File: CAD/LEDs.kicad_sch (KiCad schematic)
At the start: 12 parts

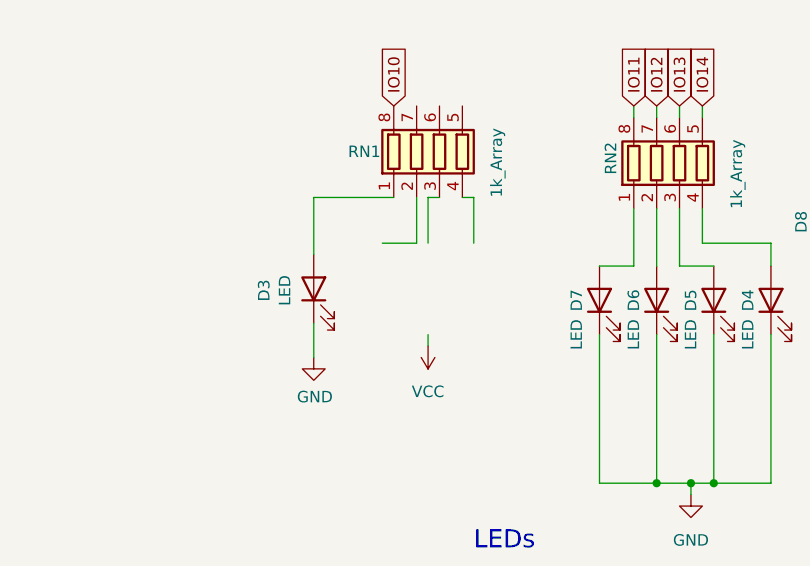
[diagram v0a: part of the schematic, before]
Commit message: Removed RN1
Removed RN1 since only one value was used. Changed to single 1k resistor
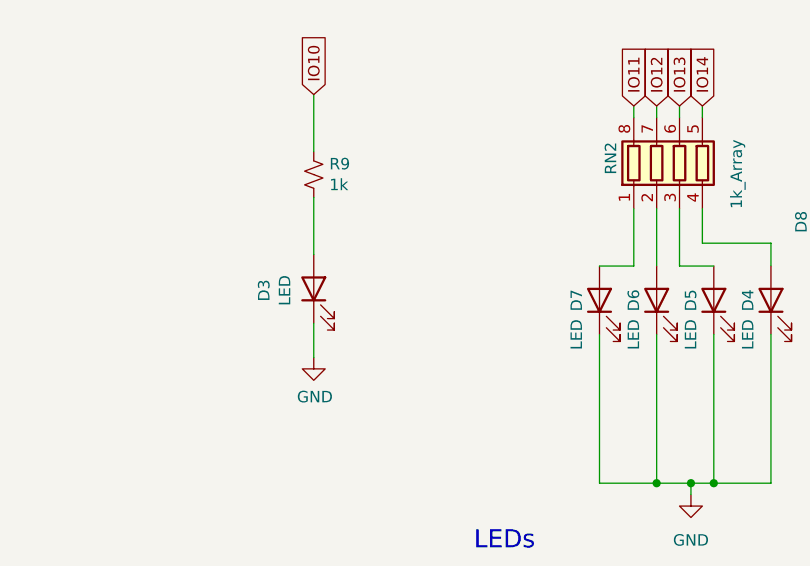
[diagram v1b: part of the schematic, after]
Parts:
- removed RN1: 1k_Array, BadgePirates:R_Array_Convex_4x0603, symbol Device:R_Pack04
- added R9: 1k, BadgePirates:R_1206_3216Metric, symbol Device:R_Small_US
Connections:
- net IO10: now also R9.1
- net at D3.2 (A): now also R9.2
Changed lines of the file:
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@@
-    (stroke (width 0) (type default))
-  )
-  (wire (pts (xy 132.08 86.36) (xy 135.89 86.36))
     (stroke (width 0) (type default))
   )
@@
     (stroke (width 0) (type default))
   )
-  (wire (pts (xy 142.24 81.28) (xy 140.97 81.28))
-    (stroke (width 0) (type default))
-  )
   (wire (pts (xy 165.1 71.12) (xy 165.1 72.39))
     (stroke (width 0) (type default))
@@
     (stroke (width 0) (type default))
   )
-  (wire (pts (xy 137.16 81.28) (xy 138.43 81.28))
-    (stroke (width 0) (type default))
-  )
   (wire (pts (xy 55.88 116.84) (xy 55.88 121.92))
     (stroke (width 0) (type default))
@@
     (stroke (width 0) (type default))
   )
+  (wire (pts (xy 124.46 69.85) (xy 124.46 76.2))
+    (stroke (width 0) (type default))
+  )
   (wire (pts (xy 160.02 88.9) (xy 160.02 82.55))
     (stroke (width 0) (type default))
@@
     (stroke (width 0) (type default))
   )
-  (wire (pts (xy 142.24 86.36) (xy 142.24 81.28))
-    (stroke (width 0) (type default))
-  )
   (wire (pts (xy 168.91 96.52) (xy 168.91 113.03))
     (stroke (width 0) (type default))
@@
     (stroke (width 0) (type default))
   )
-  (wire (pts (xy 135.89 86.36) (xy 135.89 81.28))
-    (stroke (width 0) (type default))
-  )
   (wire (pts (xy 165.1 88.9) (xy 165.1 82.55))
     (stroke (width 0) (type default))
@@
     (stroke (width 0) (type default))
   )
-  (wire (pts (xy 124.46 81.28) (xy 133.35 81.28))
-    (stroke (width 0) (type default))
-  )
   (wire (pts (xy 156.21 96.52) (xy 156.21 113.03))
     (stroke (width 0) (type default))
@@
     (stroke (width 0) (type default))
   )
-  (wire (pts (xy 137.16 96.52) (xy 137.16 97.79))
-    (stroke (width 0) (type default))
-  )
   (wire (pts (xy 55.88 121.92) (xy 35.56 121.92))
     (stroke (width 0) (type default))
@@
   )
   (wire (pts (xy 167.64 71.12) (xy 167.64 72.39))
-    (stroke (width 0) (type default))
-  )
-  (wire (pts (xy 137.16 86.36) (xy 137.16 81.28))
     (stroke (width 0) (type default))
   )
@@
     )
   )
-  (global_label "IO10" (shape input) (at 133.35 71.12 90) (fields_autoplaced)
+  (global_label "IO10" (shape input) (at 124.46 69.85 90) (fields_autoplaced)
     (effects (font (size 1.27 1.27)) (justify left))
-    (property "Intersheetrefs" "${INTERSHEET_REFS}" (at -16.51 99.06 0)
+    (property "Intersheetrefs" "${INTERSHEET_REFS}" (at -25.4 97.79 0)
       (effects (font (size 1.27 1.27)) hide)
     )
@@
     )
   )
+  (symbol (lib_id "Device:R_Small_US") (at 124.46 78.74 0) (unit 1)
+    (in_bom yes) (on_board yes) (dnp no)
+    (property "Reference" "R9" (at 126.1872 77.5716 0)
+      (effects (font (size 1.27 1.27)) (justify left))
+    )
+    (property "Value" "1k" (at 126.1872 79.883 0)
+      (effects (font (size 1.27 1.27)) (justify left))
+    )
+    (property "Footprint" "BadgePirates:R_1206_3216Metric" (at 124.46 78.74 0)
+      (effects (font (size 1.27 1.27)) hide)
+    )
+    (property "Datasheet" "~" (at 124.46 78.74 0)
+      (effects (font (size 1.27 1.27)) hide)
+    )
+    (property "OrderURL" "" (at 124.46 78.74 0)
+      (effects (font (size 1.27 1.27)) hide)
+    )
+    (pin "1")
+    (pin "2")
+    (instances
+      (project "ProjectNeoRogue"
+        (path "/76a22395-5d2d-4f66-8191-432f65fdc4ac"
+          (reference "R9") (unit 1)
+        )
+        (path "/76a22395-5d2d-4f66-8191-432f65fdc4ac/3c34205f-0c14-4e66-b000-3f846d3d7657"
+          (reference "R25") (unit 1)
+        )
+      )
+    )
+  )
   (symbol (lib_id "Device:LED") (at 124.46 91.44 90) (unit 1)
     (in_bom yes) (on_board yes) (dnp no)
@@
         (path "/76a22395-5d2d-4f66-8191-432f65fdc4ac/3c34205f-0c14-4e66-b000-3f846d3d7657"
           (reference "D4") (unit 1)
-        )
-      )
-    )
-  )
-  (symbol (lib_id "power:VCC") (at 137.16 97.79 180) (unit 1)
-    (in_bom yes) (on_board yes) (dnp no) (fields_autoplaced)
-    (property "Reference" "#PWR020" (at 137.16 93.98 0)
-      (effects (font (size 1.27 1.27)) hide)
-    )
-    (property "Value" "VCC" (at 137.16 102.87 0)
-      (effects (font (size 1.27 1.27)))
-    )
-    (property "Footprint" "" (at 137.16 97.79 0)
-      (effects (font (size 1.27 1.27)) hide)
-    )
-    (property "Datasheet" "" (at 137.16 97.79 0)
-      (effects (font (size 1.27 1.27)) hide)
-    )
-    (pin "1")
-    (instances
-      (project "ProjectNeoRogue"
-        (path "/76a22395-5d2d-4f66-8191-432f65fdc4ac"
-          (reference "#PWR020") (unit 1)
-        )
-        (path "/76a22395-5d2d-4f66-8191-432f65fdc4ac/3c34205f-0c14-4e66-b000-3f846d3d7657"
-          (reference "#PWR024") (unit 1)
         )
       )
@@
         )
       )
-    )
-  )
-  (symbol (lib_id "Device:R_Pack04") (at 138.43 76.2 0) (unit 1)
-    (in_bom yes) (on_board yes) (dnp no)
-    (property "Reference" "RN1" (at 128.27 76.2 0)
-      (effects (font (size 1.27 1.27)) (justify left))
-    )
-    (property "Value" "1k_Array" (at 144.78 81.28 90)
-      (effects (font (size 1.27 1.27)) (justify left))
-    )
-    (property "Footprint" "BadgePirates:R_Array_Convex_4x0603" (at 145.415 76.2 90)
-      (effects (font (size 1.27 1.27)) hide)
-    )
-    (property "Datasheet" "~" (at 138.43 76.2 0)
-      (effects (font (size 1.27 1.27)) hide)
-    )
-    (property "OrderURL" "" (at 138.43 76.2 0)
-      (effects (font (size 1.27 1.27)) hide)
-    )
-    (pin "1")
-    (pin "2")
-    (pin "3")
-    (pin "4")
-    (pin "5")
-    (pin "6")
-    (pin "7")
-    (pin "8")
-    (instances
-      (project "ProjectNeoRogue"
-        (path "/76a22395-5d2d-4f66-8191-432f65fdc4ac"
-          (reference "RN1") (unit 1)
-        )
-        (path "/76a22395-5d2d-4f66-8191-432f65fdc4ac/3c34205f-0c14-4e66-b000-3f846d3d7657"
-          (reference "RN1") (unit 1)
-        )
-      )

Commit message: updates
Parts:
- D1: symbol LED:WS2812B -> BadgePirates:LED_RGB_WS2812B; MFG (none) -> Worldsemi; MFG_PN (none) -> WS2812B-B/T; Vendor1 (none) -> LCSC; Vendor1_PN (none) -> C2761795; Vendor1_URL (none) -> https://www.lcsc.com/product-detail/Light-Emitting-Diodes-L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
- D3: MFG (none) -> KingBright; MFG_PN (none) -> AA3528SYCKT09; Vendor1 (none) -> Mouser; Vendor1_PN (none) -> 604-AA3528SYCKT09; Vendor1_URL (none) -> https://www.mouser.com/ProductDetail/Kingbright/AA3528SYCKT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
- D4, D5, D6, D7, D8: symbol Device:LED -> BadgePirates:LED_Yellow_ReverseMount_Gullwing; MFG (none) -> KingBright; MFG_PN (none) -> AA3528SYCKT09; Vendor1 (none) -> Mouser; Vendor1_PN (none) -> 604-AA3528SYCKT09; Vendor1_URL (none) -> https://www.mouser.com/ProductDetail/Kingbright/AA3528SYCKT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
- R9: symbol Device:R_Small_US -> BadgePirates:R_1k_1206; MFG (none) -> YAGEO; MFG_PN (none) -> RC1206FR-071KL; Vendor1 (none) -> LCSC; Vendor1_PN (none) -> C131398; Vendor1_URL (none) -> https://www.lcsc.com/product-detail/Chip-Resistor-Surface-M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
- RN2: MFG (none) -> YAGEO; MFG_PN (none) -> YC164-JR-071KL; Vendor1 (none) -> LCSC; Vendor1_PN (none) -> C93675; Vendor1_URL (none) -> https://www.lcsc.com/product-detail/Resistor-Networks-Array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
